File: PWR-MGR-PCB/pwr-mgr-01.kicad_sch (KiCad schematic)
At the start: 26 parts, among them J3 USB_C_Receptacle_USB2.0_14P, U1 BQ24075, U5 USBLC6-2SC6, U6 TPS631011YBGR-Pin_Corrected

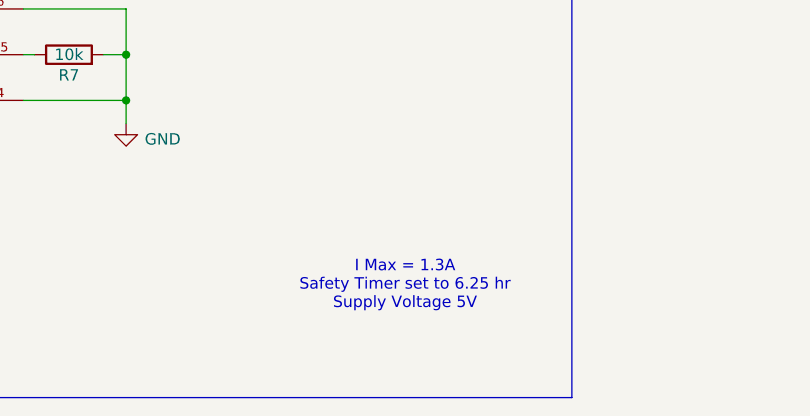
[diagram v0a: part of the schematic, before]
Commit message: align ports
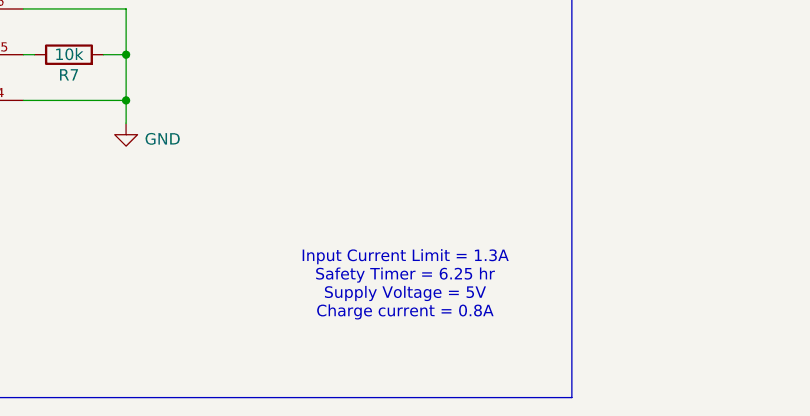
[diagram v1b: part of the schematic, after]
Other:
- note added: "Input Current Limit = 1.3A Safety Timer = 6.25 hr Supply Voltage = 5V Charge current = 0.8A"
- note removed: "I Max = 1.3A Safety Timer set to 6.25 hr Supply Voltage 5V"
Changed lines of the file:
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@@
 		)
 	)
-	(text "I Max = 1.3A\nSafety Timer set to 6.25 hr\nSupply Voltage 5V"
+	(text "Input Current Limit = 1.3A\nSafety Timer = 6.25 hr\nSupply Voltage = 5V\nCharge current = 0.8A"
 		(exclude_from_sim no)
 		(at 145.288 183.134 0)
@@
 		)
 		(instances
-			(project ""
+			(project "PWR-MGR-PCB"
 				(path "/16b2e4e2-6399-42b6-a8e6-a11780888710/aa25d2a4-7317-40e7-833e-e05b81834ee4"
 					(reference "NT1")
@@
 		)
 		(instances
-			(project ""
+			(project "PWR-MGR-PCB"
 				(path "/16b2e4e2-6399-42b6-a8e6-a11780888710/aa25d2a4-7317-40e7-833e-e05b81834ee4"
 					(reference "U1")
